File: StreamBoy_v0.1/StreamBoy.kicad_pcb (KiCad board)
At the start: 2 copper layers, 55 parts, among them J1 GB-CART, U1 XC6SLX9-TQG144, U2 LSF0204PWR, U3 LSF0204PWR

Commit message: Bunch of stuff
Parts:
- added IC1: LY68L6400SLIT, LY68L6400SLIT:SOIC127P600X175-8N, F.Cu at (154.9, 93.5)
- added J2: USB_B_Micro, Connector_USB:USB_Micro-B_Molex_47346-0001, F.Cu at (194.7, 67.4)
- added SW_RESET_GB1: SW_Push, Button_Switch_THT:SW_PUSH_6mm, F.Cu at (226.7, 68.1)
- added U4: CP2102N-A01-GQFN24, Package_DFN_QFN:QFN-24-1EP_4x4mm_P0.5mm_EP2.6x2.6mm, F.Cu at (177.8, 96.0)
- moved JPOWER3V1 89.5 mm to (237.6, 68.4)
- moved JUART1 79.3 mm to (222.4, 68.4)
- moved JTAG_ESP1 79.3 mm to (217.7, 68.4)
- moved JPOWER5V1 77.3 mm to (231.7, 76.9)
- moved JDAC1 67.5 mm to (227.0, 76.9)
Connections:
- J1 pad 31: ESP_DAC1 -> GB_VIN

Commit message: Bunch of stuff
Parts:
- added C1: C, Capacitor_SMD:C_0805_2012Metric, F.Cu at (104.6, 82.3)
- added C10: C, Capacitor_SMD:C_0805_2012Metric, F.Cu at (118.9, 69.0)
- added C2: C, Capacitor_SMD:C_0805_2012Metric, F.Cu at (104.6, 85.2)
- added C3: C, Capacitor_SMD:C_0805_2012Metric, F.Cu at (109.1, 82.3)
- added C4: C, Capacitor_SMD:C_0805_2012Metric, F.Cu at (104.6, 88.2)
- added C5: C, Capacitor_SMD:C_0805_2012Metric, F.Cu at (119.3, 59.9)
- added C6: C, Capacitor_SMD:C_0805_2012Metric, F.Cu at (114.5, 69.0)
- added C7: C, Capacitor_SMD:C_0805_2012Metric, F.Cu at (119.3, 62.9)
- added C8: C, Capacitor_SMD:C_0805_2012Metric, F.Cu at (123.7, 59.9)
- added C9: C, Capacitor_SMD:C_0805_2012Metric, F.Cu at (119.3, 65.8)
- added D1: D_Zener, b240a-13-f:DIOM5136X261N, F.Cu at (162.1, 67.1)
- added D2: D_Zener, b240a-13-f:DIOM5136X261N, F.Cu at (170.6, 67.1)
- added D3: D, Diode_SMD:D_0805_2012Metric, F.Cu at (127.0, 82.3)
- added L1: INDUCTOR, Inductor_SMD:L_0805_2012Metric, F.Cu at (109.1, 85.2)
- added L2: INDUCTOR, Inductor_SMD:L_0805_2012Metric, F.Cu at (113.5, 82.3)
- added Q1: SS8050-G, SS8050-G:SOT95P240X115-3N, F.Cu at (114.7, 60.7)
- added Q2: SS8050-G, SS8050-G:SOT95P240X115-3N, F.Cu at (114.7, 65.3)
- added R1: R, Resistor_SMD:R_0805_2012Metric, F.Cu at (109.1, 88.2)
- added R43: R, Resistor_SMD:R_0805_2012Metric, F.Cu at (113.5, 85.2)
- added R44: R, Resistor_SMD:R_0805_2012Metric, F.Cu at (117.9, 82.3)
- added R45: R, Resistor_SMD:R_0805_2012Metric, F.Cu at (113.5, 88.2)
- added R46: R, Resistor_SMD:R_0805_2012Metric, F.Cu at (117.9, 85.2)
- added R47: R, Resistor_SMD:R_0805_2012Metric, F.Cu at (123.7, 62.9)
- added R48: R, Resistor_SMD:R_0805_2012Metric, F.Cu at (128.2, 59.9)
- added R49: R, Resistor_SMD:R_0805_2012Metric, F.Cu at (123.7, 65.8)
- added R50: R, Resistor_SMD:R_0805_2012Metric, F.Cu at (123.3, 68.8)
- added R51: R, Resistor_SMD:R_0805_2012Metric, F.Cu at (128.2, 62.9)
- added U5: TPS62170DSG, Package_SON:WSON-8-1EP_2x2mm_P0.5mm_EP0.9x1.6mm_ThermalVias, F.Cu at (152.4, 72.1)
- added U6: TPS62170DSG, Package_SON:WSON-8-1EP_2x2mm_P0.5mm_EP0.9x1.6mm_ThermalVias, F.Cu at (163.8, 71.5)
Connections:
- J1 pad 1: VCC5 -> Net-(D3-Pad2)

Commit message: Brute force stuff onto a pcb
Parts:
- removed the C1 at (104.6, 82.3)
- removed the C1 at (203.2, 137.2)
- removed the C2 at (104.6, 85.2)
- removed the C2 at (198.8, 137.2)
- removed the C3 at (109.1, 82.3)
- removed the C3 at (203.2, 140.1)
- removed J2: USB_B_Micro, Connector_USB:USB_Micro-B_Molex_47346-0001
- removed the R1 at (109.1, 88.2)
- removed the R1 at (198.8, 140.1)
- removed R20, R22, R24, R26, R28, R30, R32, R34, R36, R38, R40: 10K, Resistor_SMD:R_0805_2012Metric
- removed R21, R23, R25, R27, R29, R31, R33, R35, R37, R39, R41: 20K, Resistor_SMD:R_0805_2012Metric
- removed R43, R44, R45, R46, R47, R48, R49, R50, R51: R, Resistor_SMD:R_0805_2012Metric
- removed SW_RESET_GB1: SW_Push, Button_Switch_THT:SW_PUSH_6mm
- removed U2: LSF0204PWR, LSF0204PWR:SOP65P640X120-14N
- added C1: 0.1uF, Capacitor_SMD:C_0805_2012Metric, F.Cu at (63.2, 167.8)
- added C11: 4.7uF, Capacitor_SMD:C_0805_2012Metric, F.Cu at (31.6, 140.1)
- added C12: 0.47uF, Capacitor_SMD:C_0805_2012Metric, F.Cu at (36.4, 140.2)
- added C13: 0.47uF, Capacitor_SMD:C_0805_2012Metric, F.Cu at (59.1, 158.8)
- added C14: 4.7uF, Capacitor_SMD:C_0805_2012Metric, F.Cu at (59.1, 167.1)
- added C15: 100uF, Capacitor_SMD:C_0805_2012Metric, F.Cu at (59.1, 163.2)
- added C16: 0.47uF, Capacitor_SMD:C_0805_2012Metric, F.Cu at (67.4, 156.0)
- added C17: 4.7uF, Capacitor_SMD:C_0805_2012Metric, F.Cu at (67.4, 151.8)
- added C18: 4.7uF, Capacitor_SMD:C_0805_2012Metric, F.Cu at (67.4, 147.4)
- added C19: 0.47uF, Capacitor_SMD:C_0805_2012Metric, F.Cu at (49.5, 140.3)
- added C2: 15pF, Capacitor_SMD:C_0805_2012Metric, F.Cu at (66.4, 168.1)
- added C20: 4.7uF, Capacitor_SMD:C_0805_2012Metric, F.Cu at (67.4, 142.9)
- added C21: 4.7uF, Capacitor_SMD:C_0805_2012Metric, F.Cu at (45.0, 140.3)
- added C22: 4.7uF, Capacitor_SMD:C_0805_2012Metric, F.Cu at (67.4, 139.1)
- added C23: 100uF, Capacitor_SMD:C_0805_2012Metric, F.Cu at (40.9, 140.3)
- added C24: 4.7uF, Capacitor_SMD:C_0805_2012Metric, F.Cu at (67.4, 135.3)
- added C25: 0.47uF, Capacitor_SMD:C_0805_2012Metric, F.Cu at (32.3, 163.5)
- added C26: 4.7uF, Capacitor_SMD:C_0805_2012Metric, F.Cu at (32.3, 159.4)
- added C27: 100uF, Capacitor_SMD:C_0805_2012Metric, F.Cu at (32.3, 155.3)
- added C28: 0.47uF, Capacitor_SMD:C_0805_2012Metric, F.Cu at (32.0, 152.3)
- added C29: 4.7uF, Capacitor_SMD:C_0805_2012Metric, F.Cu at (32.0, 148.5)
- added C3: 22uF, Capacitor_SMD:C_0805_2012Metric, F.Cu at (27.2, 160.7)
- added C30: 100uF, Capacitor_SMD:C_0805_2012Metric, F.Cu at (32.0, 144.7)
- added C31: 0.1uF/50V, Capacitor_SMD:C_0805_2012Metric, F.Cu at (61.3, 103.5)
- added C32: 22uF/10V, Capacitor_SMD:C_0805_2012Metric, F.Cu at (61.3, 107.3)
- added C33: 0.1uF/50V, Capacitor_SMD:C_0805_2012Metric, F.Cu at (65.7, 107.3)
- added D4: LED, LED_SMD:LED_1210_3225Metric, F.Cu at (55.2, 85.1)
- added D5: LED, LED_SMD:LED_1210_3225Metric, F.Cu at (67.9, 85.2)
- added D6: LED, LED_SMD:LED_1210_3225Metric, F.Cu at (61.6, 85.1)
- added JFPGAI2C1: Conn_01x02, Connector_PinHeader_2.54mm:PinHeader_1x02_P2.54mm_Vertical, F.Cu at (47.0, 135.3)
- added JFPGASPI1: Conn_01x04, Connector_PinHeader_2.54mm:PinHeader_1x04_P2.54mm_Vertical, F.Cu at (51.6, 133.9)
- added JPOWER1V2: Conn_01x02, Connector_PinHeader_2.54mm:PinHeader_1x02_P2.54mm_Vertical, F.Cu at (36.8, 135.3)
- added JRESET1: Conn_01x02, Connector_PinHeader_2.54mm:PinHeader_1x02_P2.54mm_Vertical, F.Cu at (43.2, 87.0)
- added JSD1: Micro_SD_Card, TF-015:TF015, F.Cu at (28.6, 120.0)
- added JUSB1: USB_B_Micro, Connector_USB:USB_Micro-B_Molex_47346-0001, F.Cu at (24.8, 106.7)
- added R1: 75K, Resistor_SMD:R_0805_2012Metric, F.Cu at (27.2, 156.9)
- added SW_B1: SW_Push, Button_Switch_THT:SW_PUSH_6mm, F.Cu at (27.4, 84.3)
- added SW_B2: SW_Push, Button_Switch_THT:SW_PUSH_6mm, F.Cu at (33.0, 90.8)
- added U10: TPS62170DSG, Package_SON:WSON-8-1EP_2x2mm_P0.5mm_EP0.9x1.6mm_ThermalVias, F.Cu at (25.3, 165.5)
- added U11: TPS62170DSG, Package_SON:WSON-8-1EP_2x2mm_P0.5mm_EP0.9x1.6mm_ThermalVias, F.Cu at (25.5, 151.3)
- added U12: CP2102N-A01-GQFN28, Package_DFN_QFN:QFN-28-1EP_5x5mm_P0.5mm_EP3.35x3.35mm, F.Cu at (34.9, 106.7)
- added U7: LSF0204PWR, LSF0204PWR:SOP65P640X120-14N, F.Cu at (45.7, 175.0)
- added U8: LSF0204PWR, LSF0204PWR:SOP65P640X120-14N, F.Cu at (52.1, 175.0)
- added U9: LSF0204PWR, LSF0204PWR:SOP65P640X120-14N, F.Cu at (26.6, 175.0)
- added X1: SG-7050CBN, Oscillator:Oscillator_SMD_SeikoEpson_SG8002CA-4Pin_7.0x5.0mm, F.Cu at (64.8, 161.5)
- C10, C8: value C -> 0.1uF
- C4, C5: value C -> 10uF
- C6: value C -> 22uF
- C7: value C -> 1uF
- C9: value C -> 4.7uF
- D1, D2: value D_Zener -> D; footprint b240a-13-f:DIOM5136X261N -> Diode_SMD:D_0805_2012Metric
- D3: value D -> LED; footprint Diode_SMD:D_0805_2012Metric -> LED_SMD:LED_1210_3225Metric
- JUART1: value Conn_01x04 -> Conn_01x06; footprint Connector_PinHeader_2.54mm:PinHeader_1x04_P2.54mm_Vertical -> Connector_PinHeader_2.54mm:PinHeader_1x06_P2.54mm_Vertical
- L1, L2: value INDUCTOR -> 2.2uH
- R11: value 20K -> 2K
- R13, R15, R17, R19: value 20K -> 4.7K
- R14, R18: value 10K -> 4.7K
- R16: value 10K -> 10k
- R2: value 10K -> 24K
- R3: value 20K -> 100KOhm
- R4: value 10K -> 75K
- R5: value 20K -> 4.7KOhm
- R6, R8: value 10K -> 4.7KOhm
- R7: value 20K -> 150K
- R9: value 20K -> 10K
- U4: value CP2102N-A01-GQFN24 -> LSF0204PWR; footprint Package_DFN_QFN:QFN-24-1EP_4x4mm_P0.5mm_EP2.6x2.6mm -> LSF0204PWR:SOP65P640X120-14N
- U5, U6: value TPS62170DSG -> LSF0204PWR; footprint Package_SON:WSON-8-1EP_2x2mm_P0.5mm_EP0.9x1.6mm_ThermalVias -> LSF0204PWR:SOP65P640X120-14N
- moved JPOWER3V1 217.6 mm to (30.5, 135.1), turned to 180 degrees
- moved JPOWER5V1 214.9 mm to (24.1, 132.6)
- moved JUART1 189.2 mm to (35.6, 98.4), turned to 270 degrees
- moved JDAC1 173.1 mm to (63.2, 132.8)
- moved JTAG_ESP1 169.6 mm to (50.8, 98.4), turned to 270 degrees
- moved U6 161.9 mm to (39.3, 175.0), turned to 270 degrees
- moved U5 157.6 mm to (33.0, 175.0), turned to 270 degrees
- moved R18 154.8 mm to (25.1, 94.6), turned to 180 degrees
- moved R19 148.4 mm to (35.3, 94.6), turned to 180 degrees
- moved R3 147.5 mm to (21.8, 164.9), turned to 90 degrees
- moved D2 145.4 mm to (29.8, 103.5), turned to 180 degrees
- moved R2 139.3 mm to (24.0, 156.9), turned to 270 degrees
- moved D1 138.8 mm to (29.8, 109.2), turned to 180 degrees
- moved R10 138.3 mm to (40.6, 106.7), turned to 180 degrees
- moved R4 138.1 mm to (24.3, 142.4), turned to 90 degrees
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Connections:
- A1 pad 1: Net-(A1-Pad1) -> GND
- A1 pad 10: Net-(A1-Pad10) -> ESP_DAC1
- A1 pad 11: Net-(A1-Pad11) -> ESP_FPGA_CS
- A1 pad 12: Net-(A1-Pad12) -> ESP_LED2
- A1 pad 13: Net-(A1-Pad13) -> ESP_JTAG_MTMS
- A1 pad 14: Net-(A1-Pad14) -> ESP_JTAG_MTDI
- A1 pad 15: Net-(A1-Pad1) -> GND
- A1 pad 16: Net-(A1-Pad16) -> ESP_JTAG_MTCK
- A1 pad 2: Net-(A1-Pad2) -> VCC3
- A1 pad 23: Net-(A1-Pad23) -> ESP_JTAG_MTDO
- A1 pad 25: Net-(A1-Pad25) -> ESP_IO0
- A1 pad 26: Net-(A1-Pad26) -> ESP_GB_RESET
- A1 pad 29: Net-(A1-Pad29) -> ESP_SD_CS
- A1 pad 3: Net-(A1-Pad3) -> ESP_EN
- A1 pad 30: Net-(A1-Pad30) -> ESP_FPGA_SCLK
- A1 pad 31: Net-(A1-Pad31) -> ESP_FPGA_MISO
- A1 pad 33: Net-(A1-Pad33) -> ESP_I2C_SCL
- A1 pad 34: Net-(A1-Pad34) -> ESP_RX
- A1 pad 35: Net-(A1-Pad35) -> ESP_TX
- A1 pad 36: Net-(A1-Pad36) -> ESP_I2C_SDA
- A1 pad 37: Net-(A1-Pad37) -> ESP_FPGA_MOSI
- A1 pad 38: Net-(A1-Pad1) -> GND
- A1 pad 39: Net-(A1-Pad39) -> GND
- A1 pad 6: Net-(A1-Pad6) -> ESP_BUTTON1
- A1 pad 8: Net-(A1-Pad8) -> ESP_LED1
- A1 pad 9: Net-(A1-Pad9) -> ESP_BUTTON2
- C10 pad 1: Net-(C10-Pad1) -> VCC3
- C10 pad 2: Net-(C10-Pad2) -> GND
- C4 pad 1: Net-(C4-Pad1) -> VCC5
- C4 pad 2: Net-(C4-Pad2) -> GND
- C5 pad 1: Net-(C5-Pad1) -> VCC5
- C5 pad 2: Net-(C5-Pad2) -> GND
- C6 pad 1: Net-(C6-Pad1) -> VCC1V2
- C6 pad 2: Net-(C6-Pad2) -> GND
- C7 pad 1: Net-(C7-Pad1) -> VCC3
- C7 pad 2: Net-(C7-Pad2) -> GND
- C8 pad 1: Net-(C8-Pad1) -> VCC3
- C8 pad 2: Net-(C8-Pad2) -> GND
- C9 pad 1: Net-(C9-Pad1) -> VCC3
- C9 pad 2: Net-(C9-Pad2) -> GND
- D1 pad 1: Net-(D1-Pad1) -> VCC5
- D1 pad 2: Net-(D1-Pad2) -> GB_5V
- D2 pad 1: Net-(D2-Pad1) -> VCC5
- D2 pad 2: Net-(D2-Pad2) -> USB5V
- D3 pad 1: VCC5 -> GND
- IC1 pad 1: Net-(IC1-Pad1) -> RAM_CS
- IC1 pad 2: Net-(IC1-Pad2) -> RAM_D1
- IC1 pad 3: Net-(IC1-Pad3) -> RAM_D2
- IC1 pad 4: Net-(IC1-Pad4) -> GND
- IC1 pad 5: Net-(IC1-Pad5) -> RAM_D0
- IC1 pad 6: Net-(IC1-Pad6) -> RAM_CLK
- IC1 pad 7: Net-(IC1-Pad7) -> RAM_D3
- J1 pad 1: Net-(D3-Pad2) -> GB_5V
- J1 pad 30: GB_RST -> ESP_GB_RESET
- J1 pad 31: GB_VIN -> ESP_DAC1
- JDAC1 pad 2: ESP_DAC2 -> GND
- JTAG_ESP1 pad 1: ESP_MTMS -> ESP_JTAG_MTMS
- JTAG_ESP1 pad 2: ESP_MTDI -> ESP_JTAG_MTDI
- JTAG_ESP1 pad 3: ESP_MTCK -> ESP_JTAG_MTCK
- JTAG_ESP1 pad 4: ESP_MTDO -> ESP_JTAG_MTDO
- JUART1 pad 4: GND -> ESP_DTR
- L1 pad 2: Net-(L1-Pad2) -> VCC3
- L2 pad 2: Net-(L2-Pad2) -> VCC1V2
- Q1 pad 2: Net-(Q1-Pad2) -> ESP_RTS
- Q1 pad 3: Net-(Q1-Pad3) -> ESP_EN
- Q2 pad 2: Net-(Q2-Pad2) -> ESP_DTR
- Q2 pad 3: Net-(Q2-Pad3) -> ESP_IO0
- R10 pad 1: A2 -> Net-(Q2-Pad1)
- R10 pad 2: GB_A2 -> ESP_RTS
- R11 pad 1: GND -> Net-(R11-Pad1)
- R11 pad 2: A2 -> VCC3
- R12 pad 1: RD -> Net-(R12-Pad1)
- R12 pad 2: GB_RD -> GND
- R13 pad 1: GND -> ESP_LED1
- R13 pad 2: RD -> Net-(D3-Pad2)
- R14 pad 1: A3 -> ESP_LED2
- R14 pad 2: GB_A3 -> Net-(D4-Pad2)
- R15 pad 1: GND -> FPGA_LED1
- R15 pad 2: A3 -> Net-(D5-Pad2)
- R16 pad 1: CS -> VCC3
- R16 pad 2: GB_CS -> ESP_EN
- R17 pad 1: GND -> FPGA_LED2
- R17 pad 2: CS -> Net-(D6-Pad2)
- R18 pad 1: A4 -> GND
- R18 pad 2: GB_A4 -> ESP_BUTTON1
- R19 pad 2: A4 -> ESP_BUTTON2
- R2 pad 1: A0 -> Net-(R1-Pad2)
- R2 pad 2: GB_A0 -> GND
- R3 pad 1: GND -> VCC3
- R3 pad 2: A0 -> Net-(R3-Pad2)
- R4 pad 1: CLK -> VCC1V2
- R4 pad 2: GB_CLK -> Net-(R4-Pad2)
- R42 pad 1: GB_RST -> ESP_GB_RESET
- R5 pad 1: GND -> Net-(R5-Pad1)
- R5 pad 2: CLK -> VCC3
- R6 pad 1: A1 -> VCC3
- R6 pad 2: GB_A1 -> Net-(R6-Pad2)
- R7 pad 1: GND -> Net-(R4-Pad2)
- R7 pad 2: A1 -> GND
- R8 pad 1: WR -> VCC3
- R8 pad 2: GB_WR -> Net-(R8-Pad2)
- R9 pad 1: GND -> Net-(Q1-Pad1)
- R9 pad 2: WR -> ESP_DTR
- U1 pad 100: Net-(U1-Pad100) -> RAM_D0
- U1 pad 101: Net-(U1-Pad101) -> RAM_CS
- U1 pad 102: Net-(U1-Pad102) -> RAM_CLK
- U1 pad 103: Net-(U1-Pad103) -> VCC3
- U1 pad 108: Net-(U1-Pad108) -> GND
- U1 pad 113: Net-(U1-Pad113) -> GND
- U1 pad 119: Net-(U1-Pad119) -> ESP_I2C_SCL
- U1 pad 120: Net-(U1-Pad120) -> ESP_I2C_SDA
- U1 pad 122: Net-(U1-Pad122) -> VCC3
- U1 pad 125: Net-(U1-Pad125) -> VCC3
- U1 pad 128: Net-(U1-Pad128) -> VCC1V2
- U1 pad 129: Net-(U1-Pad129) -> VCC3
- U1 pad 13: Net-(U1-Pad13) -> GND
- U1 pad 130: Net-(U1-Pad130) -> GND
- U1 pad 132: Net-(U1-Pad132) -> ESP_FPGA_MISO
- U1 pad 133: Net-(U1-Pad133) -> ESP_FPGA_MOSI
- U1 pad 134: Net-(U1-Pad134) -> ESP_FPGA_SCLK
- U1 pad 135: Net-(U1-Pad135) -> VCC3
- U1 pad 136: Net-(U1-Pad136) -> GND
- U1 pad 14: Net-(U1-Pad14) -> A3
- U1 pad 15: Net-(U1-Pad15) -> A2
- U1 pad 16: Net-(U1-Pad16) -> A1
- U1 pad 17: Net-(U1-Pad17) -> A0
- U1 pad 18: Net-(U1-Pad18) -> VCC3
- U1 pad 19: Net-(U1-Pad19) -> VCC1V2
- U1 pad 20: Net-(U1-Pad20) -> VCC3
- U1 pad 21: Net-(U1-Pad21) -> A7
- U1 pad 22: Net-(U1-Pad22) -> A6
- U1 pad 23: Net-(U1-Pad23) -> A5
- U1 pad 24: Net-(U1-Pad24) -> A4
- U1 pad 25: Net-(U1-Pad25) -> GND
- U1 pad 26: Net-(U1-Pad26) -> A11
- U1 pad 27: Net-(U1-Pad27) -> A10
- U1 pad 28: Net-(U1-Pad28) -> VCC1V2
- U1 pad 29: Net-(U1-Pad29) -> A9
- U1 pad 3: Net-(U1-Pad3) -> GND
- U1 pad 30: Net-(U1-Pad30) -> A8
- U1 pad 31: Net-(U1-Pad31) -> VCC3
- U1 pad 32: Net-(U1-Pad32) -> A15
- U1 pad 33: Net-(U1-Pad33) -> A14
- U1 pad 34: Net-(U1-Pad34) -> A13
- U1 pad 35: Net-(U1-Pad35) -> A12
- U1 pad 36: Net-(U1-Pad36) -> VCC3
- U1 pad 37: Net-(U1-Pad37) -> Net-(R6-Pad2)
- U1 pad 38: Net-(U1-Pad38) -> D0
- U1 pad 39: Net-(U1-Pad39) -> D1
- U1 pad 4: Net-(U1-Pad4) -> VCC3
- U1 pad 40: Net-(U1-Pad40) -> D2
- U1 pad 41: Net-(U1-Pad41) -> D3
- U1 pad 42: Net-(U1-Pad42) -> VCC3
- U1 pad 43: Net-(U1-Pad43) -> D4
- U1 pad 44: Net-(U1-Pad44) -> D5
- U1 pad 45: Net-(U1-Pad45) -> D6
- U1 pad 46: Net-(U1-Pad46) -> D7
- U1 pad 47: Net-(U1-Pad47) -> CLK
- U1 pad 48: Net-(U1-Pad48) -> WR
- U1 pad 49: Net-(U1-Pad49) -> GND
- U1 pad 50: Net-(U1-Pad50) -> RD
- U1 pad 51: Net-(U1-Pad51) -> CS
- U1 pad 52: Net-(U1-Pad52) -> VCC1V2
- U1 pad 53: Net-(U1-Pad53) -> VCC3
- U1 pad 54: Net-(U1-Pad54) -> GND
- U1 pad 63: Net-(U1-Pad63) -> VCC3
- U1 pad 68: Net-(U1-Pad68) -> GND
- U1 pad 71: Net-(U1-Pad71) -> Net-(R5-Pad1)
- U1 pad 72: Net-(U1-Pad72) -> Net-(R8-Pad2)
- U1 pad 76: Net-(U1-Pad76) -> VCC3
- U1 pad 77: Net-(U1-Pad77) -> GND
- U1 pad 82: Net-(U1-Pad82) -> FPGA_LED2
- U1 pad 83: Net-(U1-Pad83) -> FPGA_LED1
- U1 pad 86: Net-(U1-Pad86) -> VCC3
- U1 pad 89: Net-(U1-Pad89) -> VCC1V2
- U1 pad 90: Net-(U1-Pad90) -> VCC3
- U1 pad 91: Net-(U1-Pad91) -> GND
- U1 pad 96: Net-(U1-Pad96) -> GND
- U1 pad 97: Net-(U1-Pad97) -> RAM_D3
- U1 pad 98: Net-(U1-Pad98) -> RAM_D2
- U1 pad 99: Net-(U1-Pad99) -> RAM_D1
- U3 pad 10: GB_D7 -> GB_D0
- U3 pad 11: GB_D6 -> GB_D1
- U3 pad 12: GB_D5 -> GB_D2
- U3 pad 13: GB_D4 -> GB_D3
- U3 pad 2: D4 -> D3
- U3 pad 3: D5 -> D2
- U3 pad 4: D6 -> D1
- U3 pad 5: D7 -> D0
- U4 pad 1: Net-(U4-Pad1) -> VCC3
- U4 pad 10: Net-(U4-Pad10) -> GB_D4
- U4 pad 11: Net-(U4-Pad11) -> GB_D5
- U4 pad 12: Net-(U4-Pad12) -> GB_D6
- U4 pad 13: Net-(U4-Pad13) -> GB_D7
- U4 pad 14: Net-(U4-Pad14) -> VCC5
- U4 pad 2: Net-(U4-Pad2) -> D7
- U4 pad 3: Net-(U4-Pad3) -> D6
- U4 pad 4: Net-(U4-Pad4) -> D5
- U4 pad 5: Net-(U4-Pad5) -> D4
- U4 pad 6: Net-(U4-Pad6) -> (no net)
- U4 pad 7: Net-(U4-Pad7) -> GND
- U4 pad 8: Net-(U4-Pad8) -> VCC3
- U4 pad 9: Net-(U4-Pad9) -> (no net)
- U5 pad 1: Net-(U5-Pad1) -> VCC3
- U5 pad 2: Net-(U5-Pad2) -> A3
- U5 pad 3: Net-(U5-Pad3) -> A2
- U5 pad 4: Net-(U5-Pad4) -> A1
- U5 pad 5: Net-(U5-Pad5) -> A0
- U5 pad 6: Net-(U5-Pad6) -> (no net)
- U5 pad 7: Net-(U5-Pad7) -> GND
- U5 pad 8: Net-(U5-Pad8) -> VCC3
- U5 pad 9: Net-(U5-Pad9) -> (no net)
- U6 pad 1: Net-(U6-Pad1) -> VCC3
- U6 pad 2: Net-(U6-Pad2) -> A7
- U6 pad 3: Net-(U6-Pad3) -> A6
- U6 pad 4: Net-(U6-Pad4) -> A5
- U6 pad 5: Net-(U6-Pad5) -> A4
- U6 pad 6: Net-(U6-Pad6) -> (no net)
- U6 pad 7: Net-(U6-Pad7) -> GND
- U6 pad 8: Net-(U6-Pad8) -> VCC3
- U6 pad 9: Net-(U6-Pad9) -> (no net)

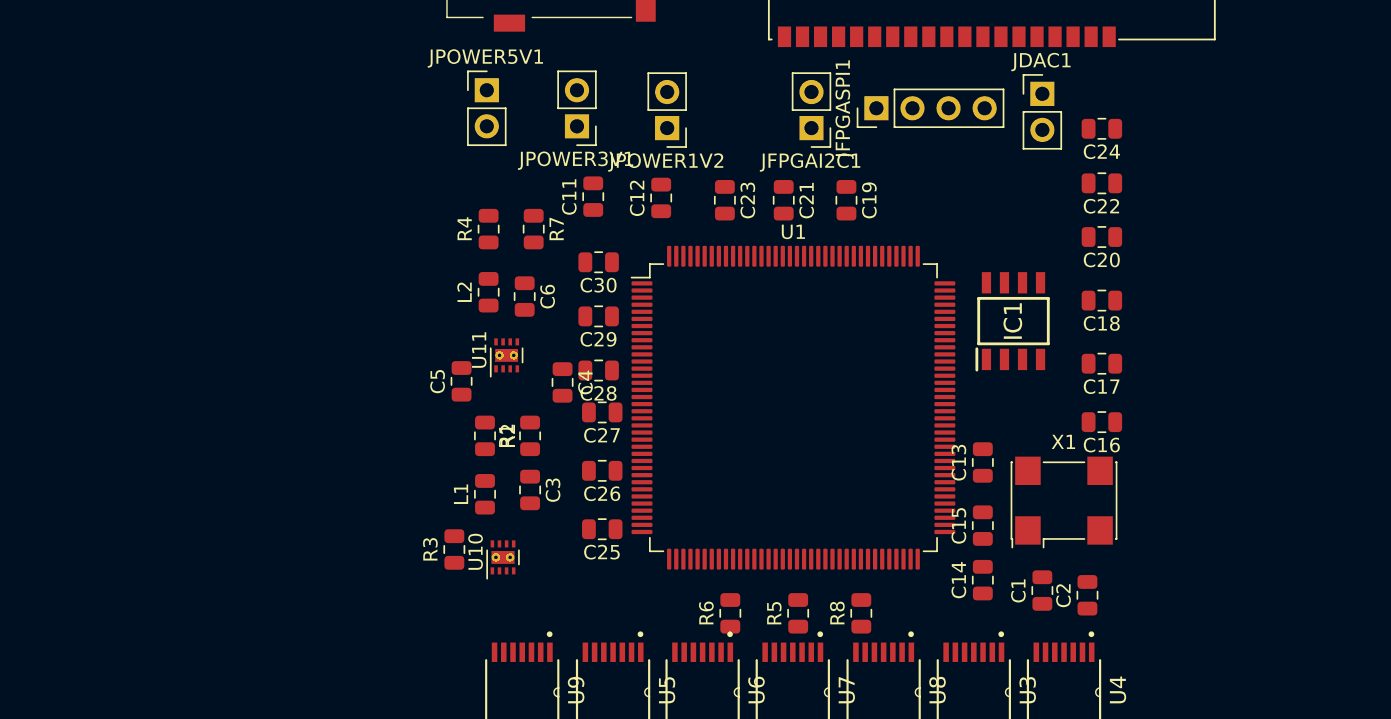
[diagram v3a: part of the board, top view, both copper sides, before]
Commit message: Added most stuff to fpga
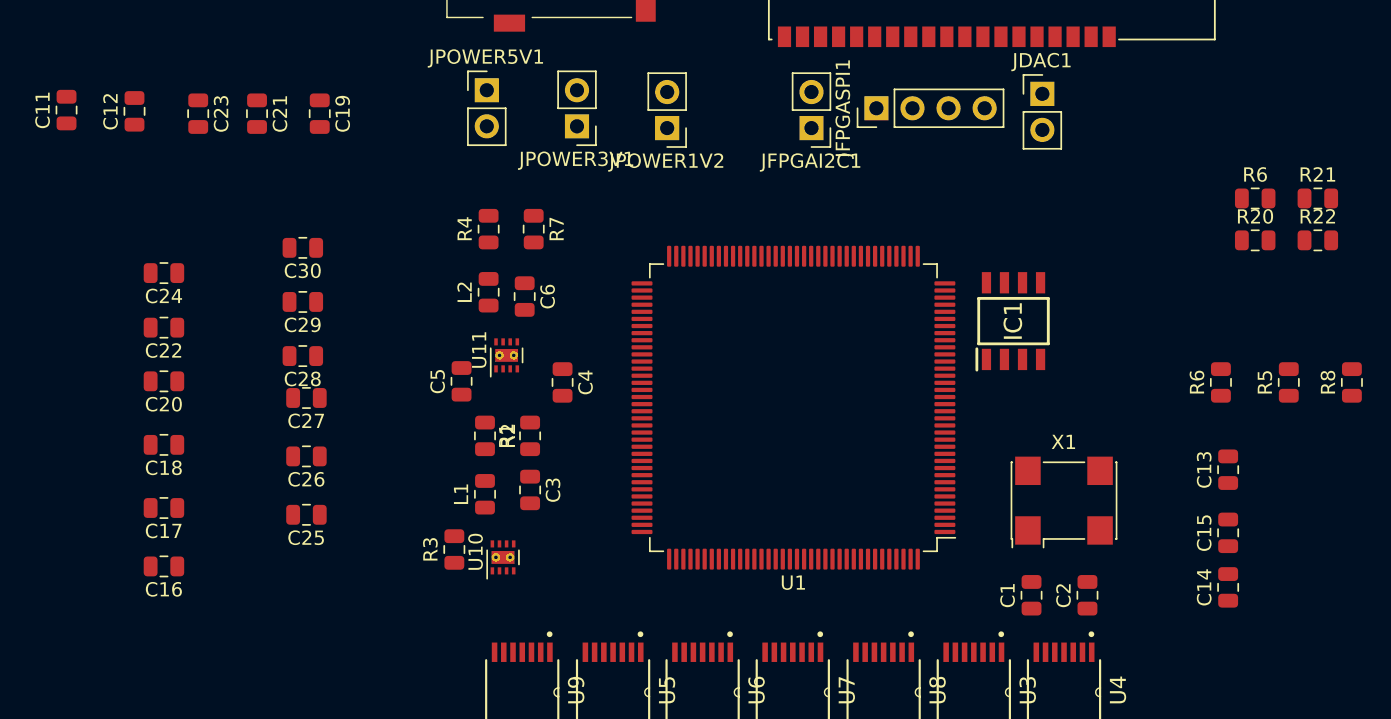
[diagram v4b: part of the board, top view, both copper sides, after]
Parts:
- added R20: 4.7KOhm, Resistor_SMD:R_0805_2012Metric, F.Cu at (78.2, 143.2)
- added R21: 4.7KOhm, Resistor_SMD:R_0805_2012Metric, F.Cu at (82.6, 140.2)
- added R22: 4.7KOhm, Resistor_SMD:R_0805_2012Metric, F.Cu at (82.6, 143.2)
- added R6: 330Ohm, Resistor_SMD:R_0805_2012Metric, F.Cu at (78.2, 140.2)
- moved C16 66.8 mm to (1.40, 166.1)
- moved C22 66.8 mm to (1.40, 149.3)
- moved C17 66.8 mm to (1.40, 162.0)
- moved C18 66.8 mm to (1.40, 157.6)
- moved C20 66.8 mm to (1.40, 153.1)
- moved C24 66.8 mm to (1.40, 145.5)
- moved R5 38.2 mm to (80.6, 153.2)
- moved R6 38.2 mm to (75.8, 153.2)
- moved R8 38.2 mm to (85.0, 153.2)
- moved C12 37.6 mm to (-0.68, 134.1)
- moved C19 37.6 mm to (12.4, 134.2)
- moved C21 37.6 mm to (7.95, 134.2)
- moved C23 37.6 mm to (3.81, 134.2)
- moved C11 37.6 mm to (-5.46, 134.0)
- moved C25 20.9 mm to (11.4, 162.5)
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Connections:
- net Net-(U1-Pad106) renamed FPGA_JTAG_TDO
- net Net-(U1-Pad107) renamed FPGA_JTAG_TMS
- net Net-(U1-Pad109) renamed FPGA_JTAG_TCK
- net Net-(U1-Pad110) renamed FPGA_JTAG_TDI
- R5 pad 1: Net-(R5-Pad1) -> FPGA_PROG
- U1 pad 100: RAM_D0 -> A0
- U1 pad 101: RAM_CS -> A1
- U1 pad 102: RAM_CLK -> A2
- U1 pad 104: Net-(U1-Pad104) -> A3
- U1 pad 105: Net-(U1-Pad105) -> A7
- U1 pad 116: Net-(U1-Pad116) -> A4
- U1 pad 117: Net-(U1-Pad117) -> A5
- U1 pad 118: Net-(U1-Pad118) -> A6
- U1 pad 119: ESP_I2C_SCL -> A8
- U1 pad 120: ESP_I2C_SDA -> Net-(U1-Pad120)
- U1 pad 121: Net-(U1-Pad121) -> A9
- U1 pad 123: Net-(U1-Pad123) -> A10
- U1 pad 124: Net-(U1-Pad124) -> A11
- U1 pad 126: Net-(U1-Pad126) -> A12
- U1 pad 127: Net-(U1-Pad127) -> A13
- U1 pad 131: Net-(U1-Pad131) -> A14
- U1 pad 132: ESP_FPGA_MISO -> A15
- U1 pad 133: ESP_FPGA_MOSI -> D0
- U1 pad 134: ESP_FPGA_SCLK -> D1
- U1 pad 137: Net-(U1-Pad137) -> D2
- U1 pad 138: Net-(U1-Pad138) -> D3
- U1 pad 139: Net-(U1-Pad139) -> D4
- U1 pad 14: A3 -> Net-(U1-Pad14)
- U1 pad 140: Net-(U1-Pad140) -> D5
- U1 pad 141: Net-(U1-Pad141) -> D6
- U1 pad 142: Net-(U1-Pad142) -> D7
- U1 pad 144: Net-(U1-Pad144) -> HSWAPEN
- U1 pad 15: A2 -> Net-(U1-Pad15)
- U1 pad 16: A1 -> Net-(U1-Pad16)
- U1 pad 17: A0 -> Net-(U1-Pad17)
- U1 pad 21: A7 -> Net-(U1-Pad21)
- U1 pad 22: A6 -> Net-(U1-Pad22)
- U1 pad 23: A5 -> Net-(U1-Pad23)
- U1 pad 24: A4 -> Net-(U1-Pad24)
- U1 pad 26: A11 -> Net-(U1-Pad26)
- U1 pad 27: A10 -> Net-(U1-Pad27)
- U1 pad 29: A9 -> Net-(U1-Pad29)
- U1 pad 30: A8 -> Net-(U1-Pad30)
- U1 pad 32: A15 -> Net-(U1-Pad32)
- U1 pad 33: A14 -> FPGA_LED2
- U1 pad 34: A13 -> FPGA_LED1
- U1 pad 35: A12 -> Net-(U1-Pad35)
- U1 pad 37: Net-(R6-Pad2) -> FPGA_PROG
- U1 pad 38: D0 -> Net-(U1-Pad38)
- U1 pad 39: D1 -> INIT_B
- U1 pad 40: D2 -> Net-(U1-Pad40)
- U1 pad 41: D3 -> Net-(U1-Pad41)
- U1 pad 43: D4 -> Net-(U1-Pad43)
- U1 pad 44: D5 -> Net-(U1-Pad44)
- U1 pad 45: D6 -> Net-(U1-Pad45)
- U1 pad 46: D7 -> Net-(U1-Pad46)
- U1 pad 47: CLK -> Net-(U1-Pad47)
- U1 pad 48: WR -> Net-(U1-Pad48)
- U1 pad 50: RD -> Net-(U1-Pad50)
- U1 pad 51: CS -> Net-(U1-Pad51)
- U1 pad 56: Net-(U1-Pad56) -> ESP_I2C_SDA
- U1 pad 57: Net-(U1-Pad57) -> ESP_I2C_SCL
- U1 pad 60: Net-(U1-Pad60) -> VCC3
- U1 pad 62: Net-(U1-Pad62) -> ESP_FPGA_CS
- U1 pad 65: Net-(U1-Pad65) -> ESP_FPGA_MOSI
- U1 pad 66: Net-(U1-Pad66) -> ESP_FPGA_MISO
- U1 pad 69: Net-(U1-Pad69) -> VCC3
- U1 pad 70: Net-(U1-Pad70) -> ESP_FPGA_SCLK
- U1 pad 71: Net-(R5-Pad1) -> FPGA_DONE
- U1 pad 73: Net-(U1-Pad73) -> SUSPEND
- U1 pad 82: FPGA_LED2 -> RAM_D3
- U1 pad 83: FPGA_LED1 -> RAM_D2
- U1 pad 84: Net-(U1-Pad84) -> RAM_D1
- U1 pad 85: Net-(U1-Pad85) -> RAM_D0
- U1 pad 87: Net-(U1-Pad87) -> RAM_CS
- U1 pad 88: Net-(U1-Pad88) -> RAM_CLK
- U1 pad 92: Net-(U1-Pad92) -> FPGA_CLK_50M
- U1 pad 94: Net-(U1-Pad94) -> CS
- U1 pad 95: Net-(U1-Pad95) -> CLK
- U1 pad 97: RAM_D3 -> WR
- U1 pad 98: RAM_D2 -> RD
- U1 pad 99: RAM_D1 -> Net-(U1-Pad99)

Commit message: I hate component placement!
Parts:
- removed the R6 at (78.2, 140.2)
- removed the R6 at (75.8, 153.2)
- added R6: 330Ohm, Resistor_SMD:R_0402_1005Metric, F.Cu at (35.8, 141.2)
- C1, C11, C12, C13, C14, C15, C16, C17, C18, C19, C2, C20, C21, C22, C23, C24, C25, C26, C27, C28, C29, C30, C4, C5: footprint Capacitor_SMD:C_0805_2012Metric -> Capacitor_SMD:C_0402_1005Metric
- C3, C6: footprint Capacitor_SMD:C_0805_2012Metric -> Capacitor_SMD:C_0603_1608Metric
- R1, R2, R20, R21, R22, R3, R4, R5, R7, R8: footprint Resistor_SMD:R_0805_2012Metric -> Resistor_SMD:R_0402_1005Metric
- R13, R14, R15, R17, R18, R19: value 4.7K -> 4.7KOhm
- moved C24 67.9 mm to (65.3, 168.4), turned to 90 degrees
- moved C22 64.8 mm to (64.0, 166.1), turned to 90 degrees
- moved C16 63.9 mm to (65.3, 166.1), turned to 270 degrees
- moved C17 62.9 mm to (64.0, 168.4), turned to 270 degrees
- moved C20 62.7 mm to (62.7, 166.1), turned to 90 degrees
- moved C18 62.3 mm to (62.7, 168.4), turned to 270 degrees
- moved D1 59.2 mm to (23.9, 168.1)
- moved C11 55.9 mm to (50.0, 141.0), turned to 270 degrees
- moved R8 50.4 mm to (35.8, 142.2), turned to 0 degrees
- moved C12 49.9 mm to (48.8, 141.0), turned to 270 degrees
- moved C28 48.9 mm to (59.6, 144.6), turned to 0 degrees
- moved R22 48.9 mm to (33.8, 143.8), turned to 90 degrees
- moved C30 48.5 mm to (59.6, 147.1), turned to 0 degrees
- moved C29 48.4 mm to (59.6, 145.8), turned to 0 degrees
- moved C13 45.8 mm to (31.2, 167.6)
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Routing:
- net VCC3: track 0.00 -> 39.3 mm, vias 0 -> 6
- net VCC1V2: track 0.00 -> 12.5 mm, vias 0 -> 3
- net Net-(L1-Pad1): track 0.00 -> 4.03 mm
- net FPGA_DONE: track 0.00 -> 3.71 mm
- net Net-(R4-Pad2): track 0.00 -> 3.45 mm
- net SUSPEND: track 0.00 -> 2.99 mm
- net Net-(R1-Pad2): track 0.00 -> 2.85 mm
- net Net-(R8-Pad2): track 0.00 -> 2.32 mm
- net VCC5: track 0.00 -> 2.16 mm

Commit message: Started to route some stuff
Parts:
- D1, D2: footprint Diode_SMD:D_0805_2012Metric -> Diode_SMD:D_SOD-123F
- moved R3 25.1 mm to (63.2, 150.9)
- moved C25 24.9 mm to (63.5, 144.5), turned to 0 degrees
- moved C26 23.5 mm to (63.5, 143.5), turned to 0 degrees
- moved C27 22.2 mm to (63.5, 142.5), turned to 0 degrees
- moved D2 13.9 mm to (40.4, 112.5), turned to 90 degrees
- moved C15 6.15 mm to (29.0, 163.8), turned to 180 degrees
- moved C30 4.64 mm to (60.1, 142.5)
- moved C14 4.48 mm to (29.0, 164.9), turned to 180 degrees
- moved R42 3.74 mm to (40.9, 117.5)
- moved C13 2.90 mm to (29.0, 165.9), turned to 180 degrees
- moved C29 2.34 mm to (60.1, 143.6)
- moved R20 2.30 mm to (56.1, 141.0), turned to 90 degrees
- moved R5 1.83 mm to (57.1, 141.0), turned to 90 degrees
- moved R21 1.37 mm to (56.1, 166.6), turned to 90 degrees
- moved D1 1.02 mm to (22.9, 168.1), turned to 270 degrees
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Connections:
- U1 pad 105: A7 -> Net-(U1-Pad105)
- U1 pad 115: Net-(U1-Pad115) -> A4
- U1 pad 116: A4 -> A5
- U1 pad 117: A5 -> A6
- U1 pad 118: A6 -> A7
- U1 pad 82: RAM_D3 -> RAM_D0
- U1 pad 83: RAM_D2 -> RAM_D3
- U1 pad 85: RAM_D0 -> RAM_D2
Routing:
- net VCC3: track 39.3 -> 162.2 mm, vias 6 -> 11
- net CS: track 0.00 -> 24.3 mm, vias 0 -> 2
- net D6: track 0.00 -> 23.4 mm, vias 0 -> 2
- net D5: track 0.00 -> 22.8 mm, vias 0 -> 2
- net D7: track 0.00 -> 22.3 mm, vias 0 -> 2
- net CLK: track 0.00 -> 21.5 mm
- net WR: track 0.00 -> 20.5 mm
- net RD: track 0.00 -> 19.9 mm
- net D4: track 0.00 -> 16.0 mm
- net A0: track 0.00 -> 14.2 mm
- net D0: track 0.00 -> 13.4 mm
- net D1: track 0.00 -> 13.4 mm
- net A1: track 0.00 -> 13.4 mm
- net RAM_D1: track 0.00 -> 12.7 mm
- net A2: track 0.00 -> 12.6 mm
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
